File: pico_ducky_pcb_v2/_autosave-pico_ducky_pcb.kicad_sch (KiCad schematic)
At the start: 31 parts, among them J1 USB_A, SW1 R-667799, SW2 R-667799, U2 W25Q32JVZP, U3 RP2040, Y1 Crystal_GND24

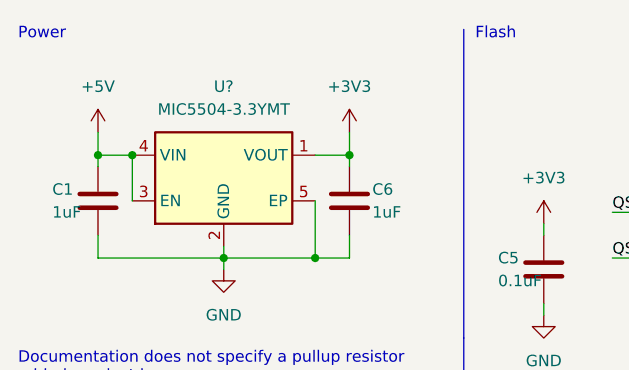
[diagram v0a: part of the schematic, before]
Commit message: fix issues with mic5504mt compoennt
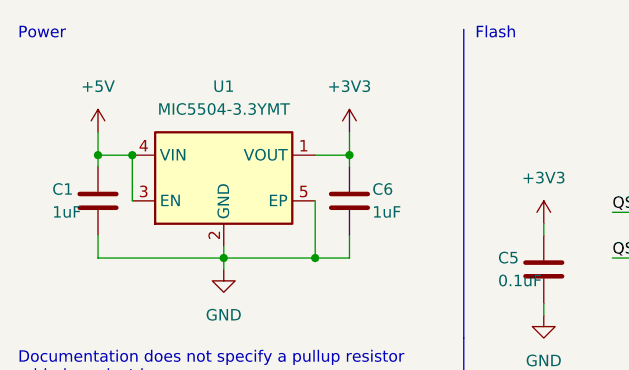
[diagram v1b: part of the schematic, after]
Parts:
- gave numbers to parts that had none: 1
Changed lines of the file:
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@@
   (symbol (lib_id "MIC5504:MIC5504-3.3YMT") (at 35.56 29.21 0) (unit 1)
     (in_bom yes) (on_board yes) (fields_autoplaced)
-    (property "Reference" "U?" (id 0) (at 35.56 19.05 0))
+    (property "Reference" "U1" (id 0) (at 35.56 19.05 0))
     (property "Value" "MIC5504-3.3YMT" (id 1) (at 35.56 21.59 0))
     (property "Footprint" "Package_DFN_QFN:UDFN-4-1EP_1x1mm_P0.65mm_EP0.48x0.48mm" (id 2) (at 35.56 39.37 0)
@@
       (reference "SW2") (unit 1) (value "R-667799") (footprint "R-WHATEVER:R-667799")
     )
+    (path "/3688ae9f-4d41-4c7d-bd3d-8b45a16022b7"
+      (reference "U1") (unit 1) (value "MIC5504-3.3YMT") (footprint "Package_DFN_QFN:UDFN-4-1EP_1x1mm_P0.65mm_EP0.48x0.48mm")
+    )
     (path "/5c0dfb3e-63f6-4ea6-b3ca-734edf20d662"
       (reference "U2") (unit 1) (value "W25Q32JVZP") (footprint "Package_SON:WSON-8-1EP_6x5mm_P1.27mm_EP3.4x4.3mm")
@@
       (reference "U3") (unit 1) (value "RP2040") (footprint "RP2040_minimal:RP2040-QFN-56")
     )
-    (path "/3688ae9f-4d41-4c7d-bd3d-8b45a16022b7"
-      (reference "U?") (unit 1) (value "MIC5504-3.3YMT") (footprint "Package_DFN_QFN:UDFN-4-1EP_1x1mm_P0.65mm_EP0.48x0.48mm")
-    )
     (path "/3d1c97c4-0ea6-49b5-8e16-2de5448ae48f"
